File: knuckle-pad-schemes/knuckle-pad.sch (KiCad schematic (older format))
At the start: 66 parts, among them SW1 SW_Push, SW10 SW_Push, SW11 SW_Push, SW12 SW_Push, SW13 SW_Push, SW14 SW_Push, SW15 SW_Push, SW16 SW_Push, SW17 SW_Push, SW18 SW_Push, SW19 SW_Push, SW2 SW_Push, SW20 SW_Push, SW21 SW_Push, SW22 SW_Push, SW23 SW_Push, SW24 SW_Push, SW25 SW_Push, SW26 SW_Push, SW27 SW_Push, SW28 SW_Push, SW29 SW_Push, SW3 SW_Push, SW4 SW_Push, SW5 SW_Push, SW6 SW_Push, SW7 SW_Push, SW8 SW_Push, SW9 SW_Push, U1 ProMicro

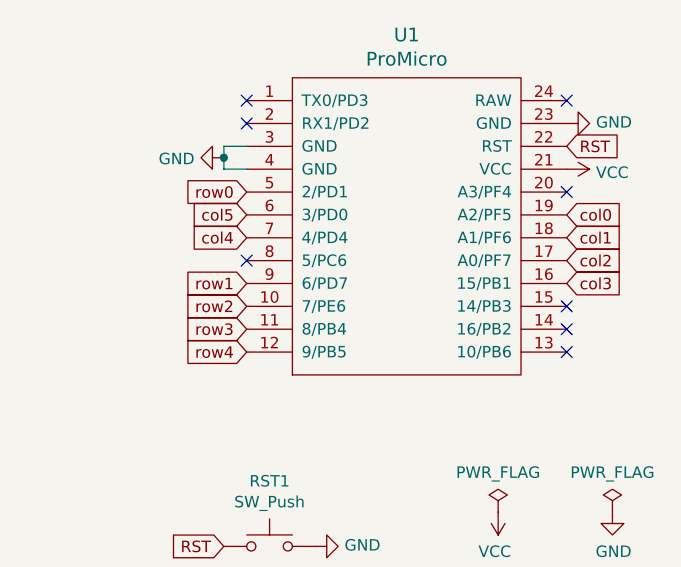
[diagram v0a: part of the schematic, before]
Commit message: v2 started -complete reroute; flipped ProMicro, changed diode footprint
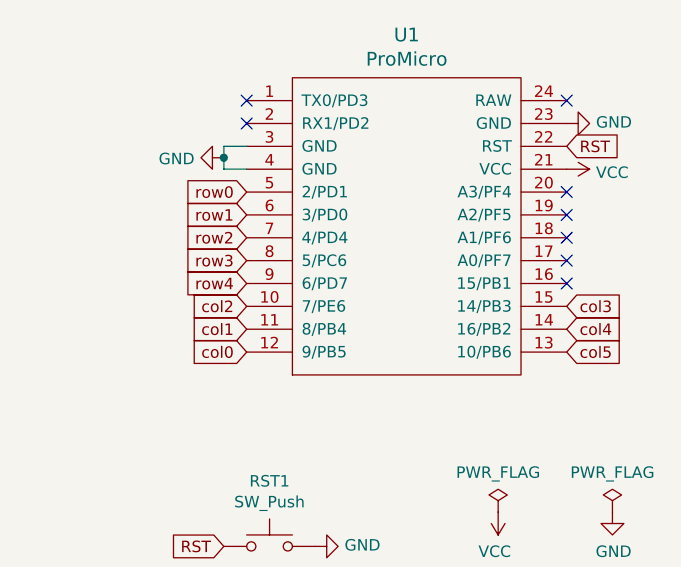
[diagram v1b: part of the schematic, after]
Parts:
- D1, D10, D11, D12, D13, D14, D15, D16, D17, D18, D19, D2, D20, D21, D22, D23, D24, D25, D26, D27, D28, D29, D3, D4, D5, D6, D7, D8, D9: footprint used_footprints:diode_TH_SMD -> acheron_Components:D_THT_7.62mm
- U1: footprint Keebio-Parts:ArduinoProMicro -> Keebio-Parts:ArduinoProMicro-ZigZag
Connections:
- net col0: now also U1.12 (9/PB5); no longer U1.19 (A2/PF5)
- net col1: now also U1.11 (8/PB4); no longer U1.18 (A1/PF6)
- net col2: now also U1.10 (7/PE6); no longer U1.17 (A0/PF7)
- net col3: now also U1.15 (14/PB3); no longer U1.16 (15/PB1)
- net col4: now also U1.14 (16/PB2); no longer U1.7 (4/PD4)
- net col5: now also U1.13 (10/PB6); no longer U1.6 (3/PD0)
- net row1: now also U1.6 (3/PD0); no longer U1.9 (6/PD7)
- net row2: now also U1.7 (4/PD4); no longer U1.10 (7/PE6)
- net row3: now also U1.8 (5/PC6); no longer U1.11 (8/PB4)
- net row4: now also U1.9 (6/PD7); no longer U1.12 (9/PB5)
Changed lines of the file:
@@
 F 0 "D1" V 1896 1330 50  0000 R CNN
 F 1 "D_Small" V 1805 1330 50  0000 R CNN
-F 2 "used_footprints:diode_TH_SMD" V 1850 1400 50  0001 C CNN
+F 2 "acheron_Components:D_THT_7.62mm" V 1850 1400 50  0001 C CNN
 F 3 "~" V 1850 1400 50  0001 C CNN
 	1    1850 1400
@@
 F 0 "D6" V 2696 1330 50  0000 R CNN
 F 1 "D_Small" V 2605 1330 50  0000 R CNN
-F 2 "used_footprints:diode_TH_SMD" V 2650 1400 50  0001 C CNN
+F 2 "acheron_Components:D_THT_7.62mm" V 2650 1400 50  0001 C CNN
 F 3 "~" V 2650 1400 50  0001 C CNN
 	1    2650 1400
@@
 F 0 "D10" V 3496 1330 50  0000 R CNN
 F 1 "D_Small" V 3405 1330 50  0000 R CNN
-F 2 "used_footprints:diode_TH_SMD" V 3450 1400 50  0001 C CNN
+F 2 "acheron_Components:D_THT_7.62mm" V 3450 1400 50  0001 C CNN
 F 3 "~" V 3450 1400 50  0001 C CNN
 	1    3450 1400
@@
 F 0 "D15" V 4296 1330 50  0000 R CNN
 F 1 "D_Small" V 4205 1330 50  0000 R CNN
-F 2 "used_footprints:diode_TH_SMD" V 4250 1400 50  0001 C CNN
+F 2 "acheron_Components:D_THT_7.62mm" V 4250 1400 50  0001 C CNN
 F 3 "~" V 4250 1400 50  0001 C CNN
 	1    4250 1400
@@
 F 0 "D20" V 4996 1330 50  0000 R CNN
 F 1 "D_Small" V 4905 1330 50  0000 R CNN
-F 2 "used_footprints:diode_TH_SMD" V 4950 1400 50  0001 C CNN
+F 2 "acheron_Components:D_THT_7.62mm" V 4950 1400 50  0001 C CNN
 F 3 "~" V 4950 1400 50  0001 C CNN
 	1    4950 1400
@@
 F 0 "D25" V 5746 1330 50  0000 R CNN
 F 1 "D_Small" V 5655 1330 50  0000 R CNN
-F 2 "used_footprints:diode_TH_SMD" V 5700 1400 50  0001 C CNN
+F 2 "acheron_Components:D_THT_7.62mm" V 5700 1400 50  0001 C CNN
 F 3 "~" V 5700 1400 50  0001 C CNN
 	1    5700 1400
@@
 F 0 "D2" V 1896 2130 50  0000 R CNN
 F 1 "D_Small" V 1805 2130 50  0000 R CNN
-F 2 "used_footprints:diode_TH_SMD" V 1850 2200 50  0001 C CNN
+F 2 "acheron_Components:D_THT_7.62mm" V 1850 2200 50  0001 C CNN
 F 3 "~" V 1850 2200 50  0001 C CNN
 	1    1850 2200
@@
 F 0 "D7" V 2696 2130 50  0000 R CNN
 F 1 "D_Small" V 2605 2130 50  0000 R CNN
-F 2 "used_footprints:diode_TH_SMD" V 2650 2200 50  0001 C CNN
+F 2 "acheron_Components:D_THT_7.62mm" V 2650 2200 50  0001 C CNN
 F 3 "~" V 2650 2200 50  0001 C CNN
 	1    2650 2200
@@
 F 0 "D11" V 3496 2130 50  0000 R CNN
 F 1 "D_Small" V 3405 2130 50  0000 R CNN
-F 2 "used_footprints:diode_TH_SMD" V 3450 2200 50  0001 C CNN
+F 2 "acheron_Components:D_THT_7.62mm" V 3450 2200 50  0001 C CNN
 F 3 "~" V 3450 2200 50  0001 C CNN
 	1    3450 2200
@@
 F 0 "D16" V 4296 2130 50  0000 R CNN
 F 1 "D_Small" V 4205 2130 50  0000 R CNN
-F 2 "used_footprints:diode_TH_SMD" V 4250 2200 50  0001 C CNN
+F 2 "acheron_Components:D_THT_7.62mm" V 4250 2200 50  0001 C CNN
 F 3 "~" V 4250 2200 50  0001 C CNN
 	1    4250 2200
@@
 F 0 "D21" V 4996 2130 50  0000 R CNN
 F 1 "D_Small" V 4905 2130 50  0000 R CNN
-F 2 "used_footprints:diode_TH_SMD" V 4950 2200 50  0001 C CNN
+F 2 "acheron_Components:D_THT_7.62mm" V 4950 2200 50  0001 C CNN
 F 3 "~" V 4950 2200 50  0001 C CNN
 	1    4950 2200
@@
 F 0 "D26" V 5746 2130 50  0000 R CNN
 F 1 "D_Small" V 5655 2130 50  0000 R CNN
-F 2 "used_footprints:diode_TH_SMD" V 5700 2200 50  0001 C CNN
+F 2 "acheron_Components:D_THT_7.62mm" V 5700 2200 50  0001 C CNN
 F 3 "~" V 5700 2200 50  0001 C CNN
 	1    5700 2200
@@
 F 0 "D3" V 1896 2930 50  0000 R CNN
 F 1 "D_Small" V 1805 2930 50  0000 R CNN
-F 2 "used_footprints:diode_TH_SMD" V 1850 3000 50  0001 C CNN
+F 2 "acheron_Components:D_THT_7.62mm" V 1850 3000 50  0001 C CNN
 F 3 "~" V 1850 3000 50  0001 C CNN
 	1    1850 3000
@@
 F 0 "D8" V 2696 2930 50  0000 R CNN
 F 1 "D_Small" V 2605 2930 50  0000 R CNN
-F 2 "used_footprints:diode_TH_SMD" V 2650 3000 50  0001 C CNN
+F 2 "acheron_Components:D_THT_7.62mm" V 2650 3000 50  0001 C CNN
 F 3 "~" V 2650 3000 50  0001 C CNN
 	1    2650 3000
@@
 F 0 "D12" V 3496 2930 50  0000 R CNN
 F 1 "D_Small" V 3405 2930 50  0000 R CNN
-F 2 "used_footprints:diode_TH_SMD" V 3450 3000 50  0001 C CNN
+F 2 "acheron_Components:D_THT_7.62mm" V 3450 3000 50  0001 C CNN
 F 3 "~" V 3450 3000 50  0001 C CNN
 	1    3450 3000
@@
 F 0 "D17" V 4296 2930 50  0000 R CNN
 F 1 "D_Small" V 4205 2930 50  0000 R CNN
-F 2 "used_footprints:diode_TH_SMD" V 4250 3000 50  0001 C CNN
+F 2 "acheron_Components:D_THT_7.62mm" V 4250 3000 50  0001 C CNN
 F 3 "~" V 4250 3000 50  0001 C CNN
 	1    4250 3000
@@
 F 0 "D22" V 4996 2930 50  0000 R CNN
 F 1 "D_Small" V 4905 2930 50  0000 R CNN
-F 2 "used_footprints:diode_TH_SMD" V 4950 3000 50  0001 C CNN
+F 2 "acheron_Components:D_THT_7.62mm" V 4950 3000 50  0001 C CNN
 F 3 "~" V 4950 3000 50  0001 C CNN
 	1    4950 3000
@@
 F 0 "D27" V 5746 2930 50  0000 R CNN
 F 1 "D_Small" V 5655 2930 50  0000 R CNN
-F 2 "used_footprints:diode_TH_SMD" V 5700 3000 50  0001 C CNN
+F 2 "acheron_Components:D_THT_7.62mm" V 5700 3000 50  0001 C CNN
 F 3 "~" V 5700 3000 50  0001 C CNN
 	1    5700 3000
@@
 F 0 "D4" V 1896 3780 50  0000 R CNN
 F 1 "D_Small" V 1805 3780 50  0000 R CNN
-F 2 "used_footprints:diode_TH_SMD" V 1850 3850 50  0001 C CNN
+F 2 "acheron_Components:D_THT_7.62mm" V 1850 3850 50  0001 C CNN
 F 3 "~" V 1850 3850 50  0001 C CNN
 	1    1850 3850
@@
 F 0 "D9" V 2696 3780 50  0000 R CNN
 F 1 "D_Small" V 2605 3780 50  0000 R CNN
-F 2 "used_footprints:diode_TH_SMD" V 2650 3850 50  0001 C CNN
+F 2 "acheron_Components:D_THT_7.62mm" V 2650 3850 50  0001 C CNN
 F 3 "~" V 2650 3850 50  0001 C CNN
 	1    2650 3850
@@
 F 0 "D13" V 3496 3780 50  0000 R CNN
 F 1 "D_Small" V 3405 3780 50  0000 R CNN
-F 2 "used_footprints:diode_TH_SMD" V 3450 3850 50  0001 C CNN
+F 2 "acheron_Components:D_THT_7.62mm" V 3450 3850 50  0001 C CNN
 F 3 "~" V 3450 3850 50  0001 C CNN
 	1    3450 3850
@@
 F 0 "D18" V 4296 3780 50  0000 R CNN
 F 1 "D_Small" V 4205 3780 50  0000 R CNN
-F 2 "used_footprints:diode_TH_SMD" V 4250 3850 50  0001 C CNN
+F 2 "acheron_Components:D_THT_7.62mm" V 4250 3850 50  0001 C CNN
 F 3 "~" V 4250 3850 50  0001 C CNN
 	1    4250 3850
@@
 F 0 "D23" V 4996 3780 50  0000 R CNN
 F 1 "D_Small" V 4905 3780 50  0000 R CNN
-F 2 "used_footprints:diode_TH_SMD" V 4950 3850 50  0001 C CNN
+F 2 "acheron_Components:D_THT_7.62mm" V 4950 3850 50  0001 C CNN
 F 3 "~" V 4950 3850 50  0001 C CNN
 	1    4950 3850
@@
 F 0 "D28" V 5746 3780 50  0000 R CNN
 F 1 "D_Small" V 5655 3780 50  0000 R CNN
-F 2 "used_footprints:diode_TH_SMD" V 5700 3850 50  0001 C CNN
+F 2 "acheron_Components:D_THT_7.62mm" V 5700 3850 50  0001 C CNN
 F 3 "~" V 5700 3850 50  0001 C CNN
 	1    5700 3850
@@
 F 0 "D5" V 1896 4680 50  0000 R CNN
 F 1 "D_Small" V 1805 4680 50  0000 R CNN
-F 2 "used_footprints:diode_TH_SMD" V 1850 4750 50  0001 C CNN
+F 2 "acheron_Components:D_THT_7.62mm" V 1850 4750 50  0001 C CNN
 F 3 "~" V 1850 4750 50  0001 C CNN
 	1    1850 4750
@@
 F 0 "D14" V 3496 4680 50  0000 R CNN
 F 1 "D_Small" V 3405 4680 50  0000 R CNN
-F 2 "used_footprints:diode_TH_SMD" V 3450 4750 50  0001 C CNN
+F 2 "acheron_Components:D_THT_7.62mm" V 3450 4750 50  0001 C CNN
 F 3 "~" V 3450 4750 50  0001 C CNN
 	1    3450 4750
@@
 F 0 "D19" V 4296 4680 50  0000 R CNN
 F 1 "D_Small" V 4205 4680 50  0000 R CNN
-F 2 "used_footprints:diode_TH_SMD" V 4250 4750 50  0001 C CNN
+F 2 "acheron_Components:D_THT_7.62mm" V 4250 4750 50  0001 C CNN
 F 3 "~" V 4250 4750 50  0001 C CNN
 	1    4250 4750
@@
 F 0 "D24" V 4996 4680 50  0000 R CNN
 F 1 "D_Small" V 4905 4680 50  0000 R CNN
-F 2 "used_footprints:diode_TH_SMD" V 4950 4750 50  0001 C CNN
+F 2 "acheron_Components:D_THT_7.62mm" V 4950 4750 50  0001 C CNN
 F 3 "~" V 4950 4750 50  0001 C CNN
 	1    4950 4750
@@
 F 0 "D29" V 5746 4680 50  0000 R CNN
 F 1 "D_Small" V 5655 4680 50  0000 R CNN
-F 2 "used_footprints:diode_TH_SMD" V 5700 4750 50  0001 C CNN
+F 2 "acheron_Components:D_THT_7.62mm" V 5700 4750 50  0001 C CNN
 F 3 "~" V 5700 4750 50  0001 C CNN
 	1    5700 4750
@@
 F 0 "U1" H 8450 2387 60  0000 C CNN
 F 1 "ProMicro" H 8450 2281 60  0000 C CNN
-F 2 "Keebio-Parts:ArduinoProMicro" V 9500 -950 60  0001 C CNN
+F 2 "Keebio-Parts:ArduinoProMicro-ZigZag" V 9500 -950 60  0001 C CNN
 F 3 "" V 9500 -950 60  0001 C CNN
 	1    8450 1550
 	1    0    0    -1
 $EndComp
-NoConn ~ 9150 1900
+NoConn ~ 9150 1800
 NoConn ~ 9150 1000
-NoConn ~ 9150 2100
-NoConn ~ 9150 2000
-NoConn ~ 7750 1700
+NoConn ~ 9150 1400
+NoConn ~ 9150 1700
+NoConn ~ 9150 1500
 NoConn ~ 7750 1000
 NoConn ~ 7750 1100
-NoConn ~ 9150 1400
+NoConn ~ 9150 1600
 Connection ~ 7650 1250
 Wire Wire Line
@@
 Text GLabel 9150 1200 2    50   Input ~ 0
 RST
+Text GLabel 9150 2100 2    50   Input ~ 0
+col5
+Text GLabel 9150 2000 2    50   Input ~ 0
+col4
+Text GLabel 9150 1900 2    50   Input ~ 0
+col3
+Text GLabel 7750 1900 0    50   Input ~ 0
+col2
+Text GLabel 7750 2000 0    50   Input ~ 0
+col1
+Text GLabel 7750 2100 0    50   Input ~ 0
+col0
+Text GLabel 7750 1800 0    50   Input ~ 0
+row4
+Text GLabel 7750 1700 0    50   Input ~ 0
+row3
+Text GLabel 7750 1600 0    50   Input ~ 0
+row2
 Text GLabel 7750 1500 0    50   Input ~ 0
-col5
-Text GLabel 7750 1600 0    50   Input ~ 0
-col4
-Text GLabel 9150 1800 2    50   Input ~ 0
-col3
-Text GLabel 9150 1700 2    50   Input ~ 0
-col2
-Text GLabel 9150 1600 2    50   Input ~ 0
-col1
-Text GLabel 9150 1500 2    50   Input ~ 0
-col0
-Text GLabel 7750 2100 0    50   Input ~ 0
-row4
-Text GLabel 7750 2000 0    50   Input ~ 0
-row3
-Text GLabel 7750 1900 0    50   Input ~ 0
-row2
-Text GLabel 7750 1800 0    50   Input ~ 0
 row1
 Text GLabel 7750 1400 0    50   Input ~ 0
